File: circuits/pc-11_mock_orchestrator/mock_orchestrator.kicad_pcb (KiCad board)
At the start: 2 copper layers, 99.1 x 99.1 mm, 39 parts, among them Q1 2N7002, Q2 2N7002, Q3 2N7002, SW1 SW_Push, SW10 SW_Push, SW11 SW_Push, SW12 SW_Push, SW13 SW_Push, SW14 SW_Push, SW15 SW_Push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

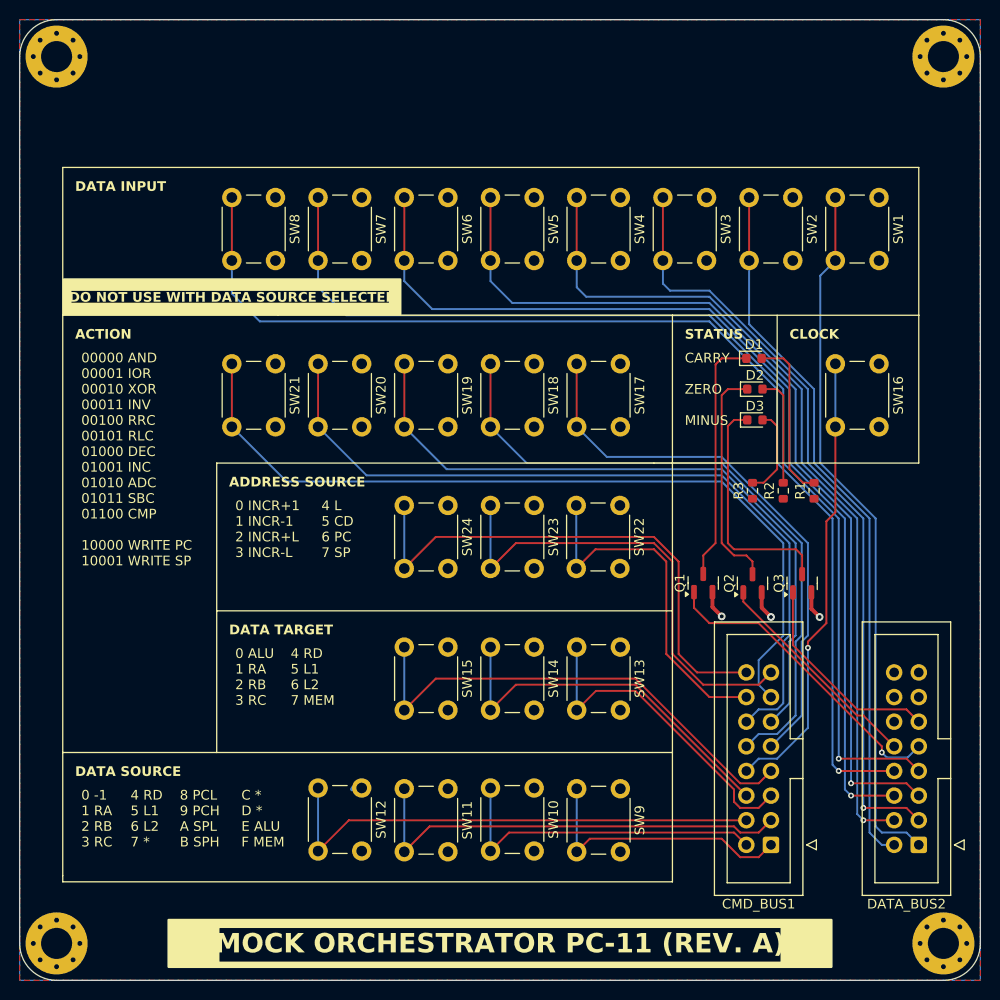
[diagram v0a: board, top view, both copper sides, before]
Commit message: add filter and decoupling capacitors to all boards
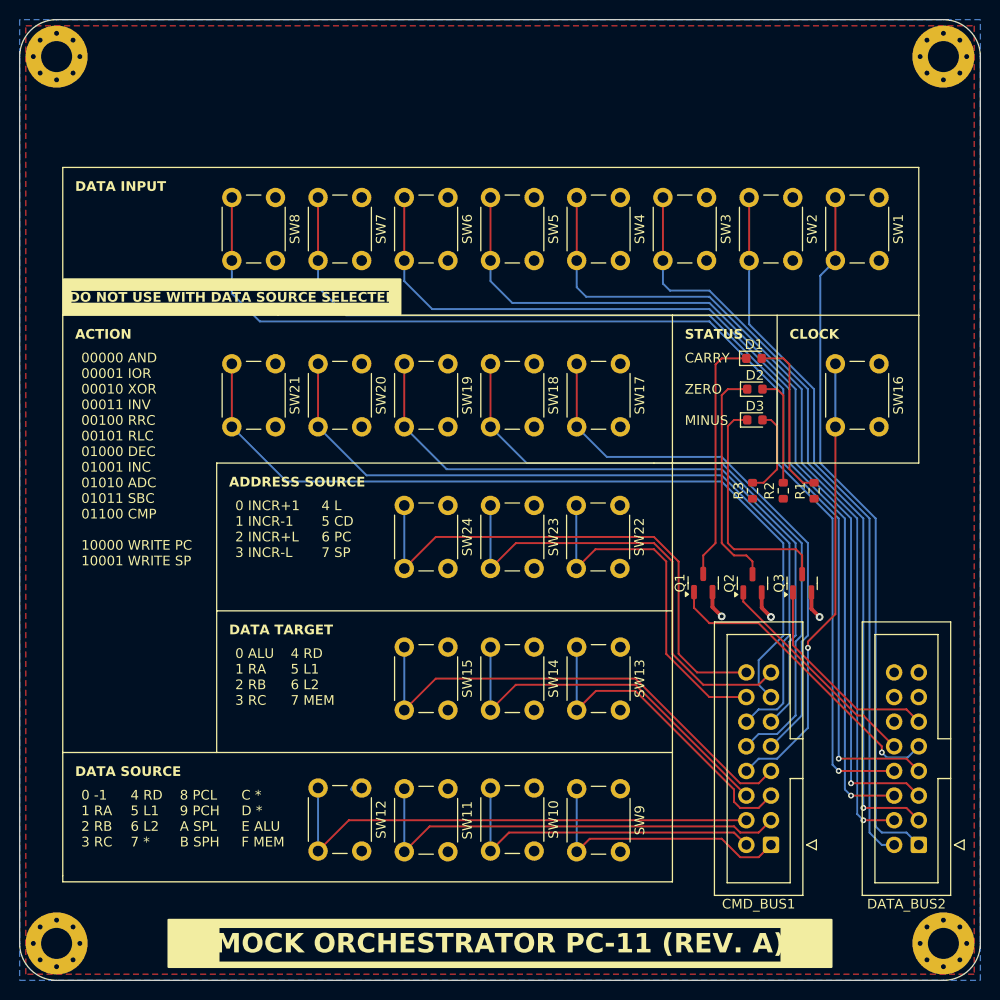
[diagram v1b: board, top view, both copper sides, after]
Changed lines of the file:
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@@
 	)
 	(segment
-		(start 123.825 74.585)
-		(end 124.75 73.66)
-		(width 0.2)
-		(layer "F.Cu")
-		(net 28)
-	)
-	(segment
-		(start 123.825 85.09)
+		(start 121.92 86.995)
+		(end 124.75 84.165)
+		(width 0.2)
+		(layer "F.Cu")
+		(net 28)
+	)
+	(segment
+		(start 124.75 84.165)
+		(end 124.75 64.845)
+		(width 0.2)
+		(layer "F.Cu")
+		(net 28)
+	)
+	(segment
+		(start 121.92 87.63)
 		(end 121.92 86.995)
-		(width 0.2)
-		(layer "F.Cu")
-		(net 28)
-	)
-	(segment
-		(start 123.825 85.09)
-		(end 123.825 74.585)
-		(width 0.2)
-		(layer "F.Cu")
-		(net 28)
-	)
-	(segment
-		(start 121.92 86.995)
-		(end 121.92 87.63)
-		(width 0.2)
-		(layer "F.Cu")
-		(net 28)
-	)
-	(segment
-		(start 124.75 73.66)
-		(end 124.75 64.845)
 		(width 0.2)
 		(layer "F.Cu")
@@
 		(polygon
 			(pts
-				(xy 40.64 22.86) (xy 139.7 22.86) (xy 139.7 121.92) (xy 40.64 121.92)
+				(xy 41.275 23.495) (xy 139.065 23.495) (xy 139.065 121.285) (xy 41.275 121.285)
 			)
 		)

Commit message: final touches, pcb ordering
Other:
- board text added: "DATA INTERCONNECT"
- board text added: "OPERATION INTERCONNECT"
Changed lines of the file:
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@@
 			(disableapertmacros no)
 			(usegerberextensions no)
-			(usegerberattributes yes)
-			(usegerberadvancedattributes yes)
-			(creategerberjobfile yes)
+			(usegerberattributes no)
+			(usegerberadvancedattributes no)
+			(creategerberjobfile no)
 			(dashed_line_dash_ratio 12.000000)
 			(dashed_line_gap_ratio 3.000000)
@@
 			(sketchdnponfab yes)
 			(crossoutdnponfab yes)
-			(subtractmaskfromsilk no)
+			(subtractmaskfromsilk yes)
 			(outputformat 1)
 			(mirror no)
-			(drillshape 1)
+			(drillshape 0)
 			(scaleselection 1)
-			(outputdirectory "")
+			(outputdirectory "./CAM")
 		)
 	)
@@
 		(tags "Through hole vertical IDC box header THT 2x08 2.54mm double row")
 		(property "Reference" "DATA_BUS2"
-			(at 1.27 -6.1 0)
+			(at 1.27 25.4 0)
 			(layer "F.SilkS")
+			(hide yes)
 			(effects
 				(font
@@
 			(at 1.27 -6.1 0)
 			(layer "F.SilkS")
+			(hide yes)
 			(effects
 				(font
@@
 		)
 	)
+	(gr_text "DATA INTERCONNECT"
+		(at 126.365 99.06 90)
+		(layer "F.SilkS")
+		(effects
+			(font
+				(size 1 1)
+				(thickness 0.1)
+			)
+			(justify bottom)
+		)
+	)
 	(gr_text "CARRY\n\nZERO\n\nMINUS"
 		(at 109.22 64.77 0)
@@
 		)
 	)
+	(gr_text "OPERATION INTERCONNECT"
+		(at 111.125 99.06 90)
+		(layer "F.SilkS")
+		(effects
+			(font
+				(size 1 1)
+				(thickness 0.1)
+			)
+			(justify bottom)
+		)
+	)

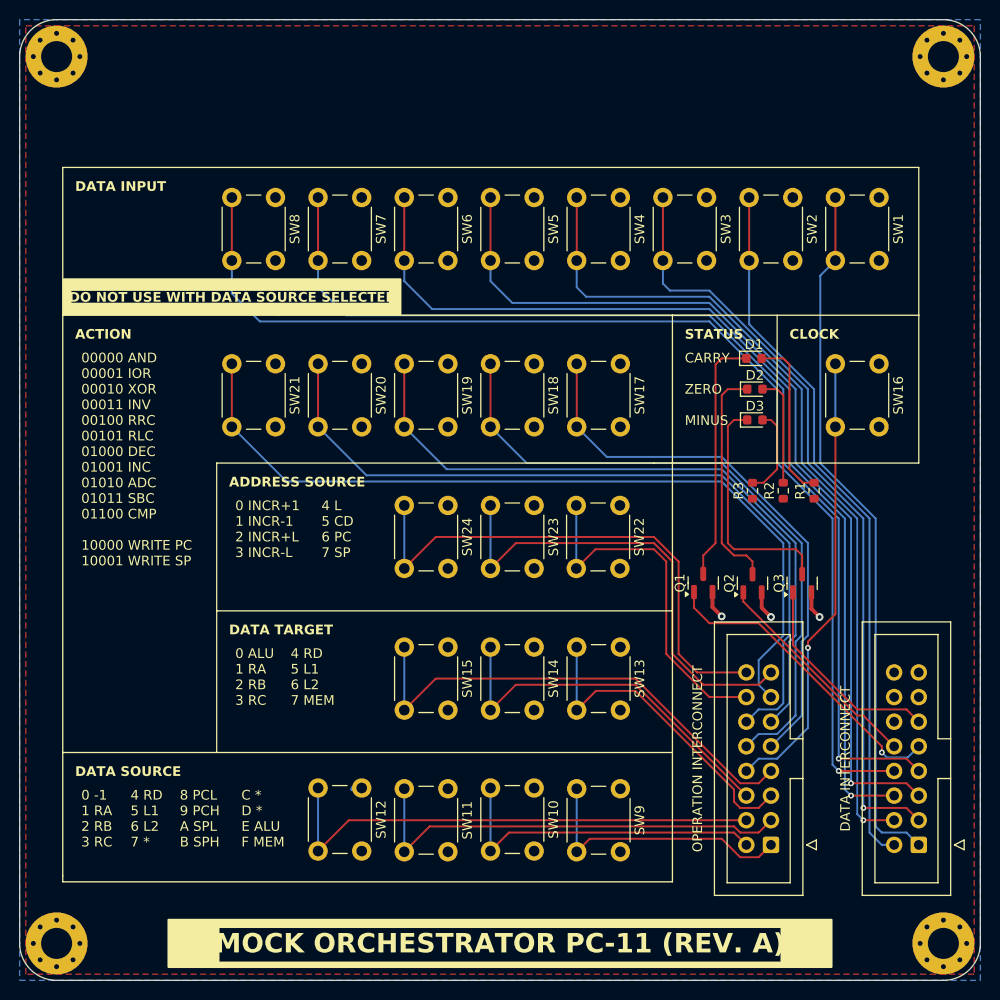
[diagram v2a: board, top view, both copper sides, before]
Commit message: update documentation and update PCBs for interrupts
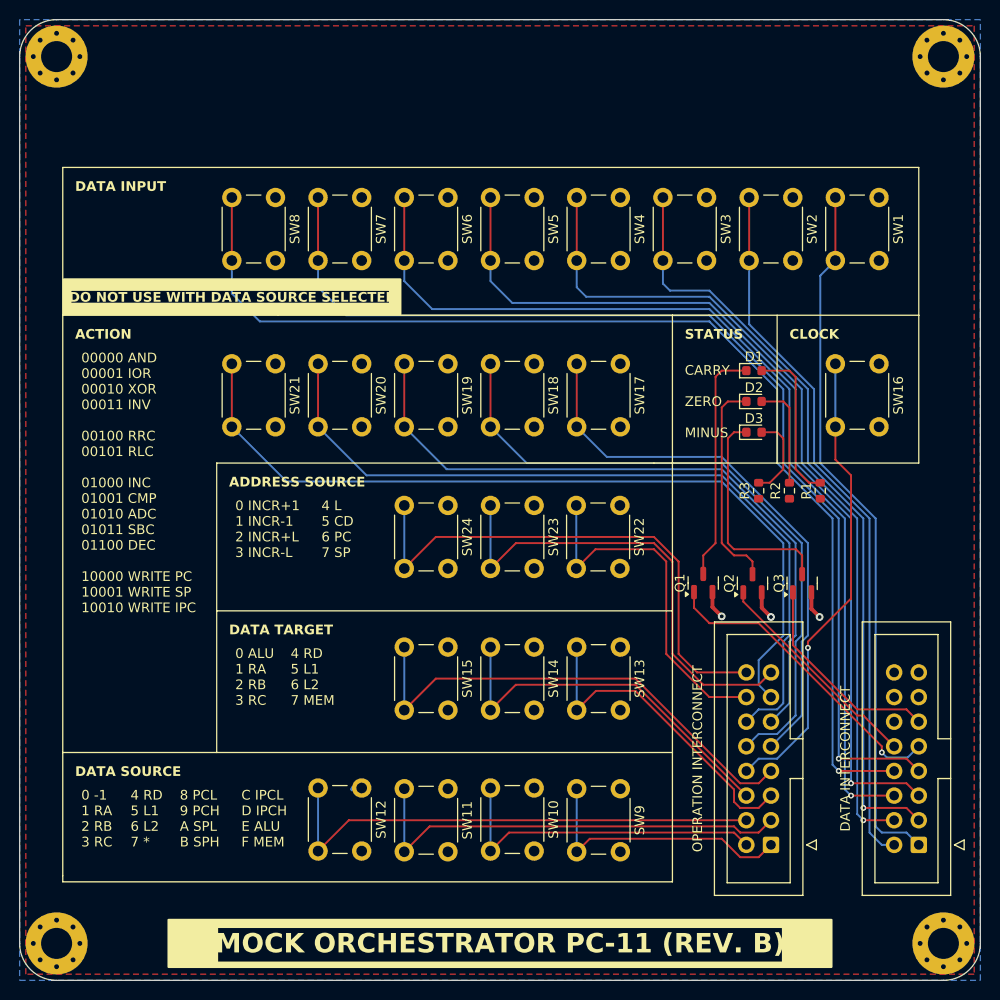
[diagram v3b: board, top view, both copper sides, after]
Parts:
- moved D2 1.27 mm to (116.4, 62.2)
- moved D3 1.27 mm to (116.4, 65.4)
- moved D1 1.27 mm to (116.4, 59.1)
- moved R2 0.64 mm to (120.0, 71.4)
- moved R3 0.64 mm to (116.8, 71.4)
- moved R1 0.63 mm to (123.2, 71.4)
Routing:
- net Net-(D3-K): track 24.4 -> 23.1 mm
- net Net-(D2-K): track 23.4 -> 22.0 mm
- net /clock: track 46.9 -> 48.2 mm
- net Net-(D1-K): track 25.6 -> 24.3 mm
- net Net-(D1-A): track 17.0 -> 16.4 mm
- net Net-(D3-A): track 9.33 -> 8.79 mm
- net Net-(D2-A): track 11.4 -> 10.9 mm
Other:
- board text added: "00000 AND 00001 IOR 00010 XOR 00011 INV 00100 RRC 00101 RLC 01000 INC 01001 CMP 01010 ADC 01011 SBC 01100 DEC 10000 WRITE PC 10001 WRITE SP 10010 WRITE IPC"
- board text added: "C IPCL D IPCH E ALU F MEM"
- board text added: "MOCK ORCHESTRATOR PC-11 (REV. B)"
- board text removed: "00000 AND 00001 IOR 00010 XOR 00011 INV 00100 RRC 00101 RLC 01000 DEC 01001 INC 01010 ADC 01011 SBC 01100 CMP 10000 WRITE PC 10001 WRITE SP"
- board text removed: "C * D * E ALU F MEM"
- board text removed: "MOCK ORCHESTRATOR PC-11 (REV. A)"
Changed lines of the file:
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@@
 	(paper "A4")
 	(title_block
-		(title "Dual 8-Bit Register Unit")
-		(date "2025-02-13")
-		(rev "PC-01-A")
+		(title "Mock Orchestrator")
+		(date "2025-11-04")
+		(rev "PC-11-B")
 	)
 	(layers
@@
 	(footprint "LED_SMD:LED_0603_1608Metric"
 		(layer "F.Cu")
-		(at 116.45 64.135)
+		(at 116.3575 65.405)
 		(descr "LED SMD 0603 (1608 Metric), square (rectangular) end terminal, IPC_7351 nominal, (Body size source: http://www.tortai-tech.com/upload/download/2011102023233369053.pdf), generated with kicad-footprint-generator")
 		(tags "LED")
@@
 	(footprint "Resistor_SMD:R_0603_1608Metric"
 		(layer "F.Cu")
-		(at 116.205 71.437 90)
+		(at 116.84 71.437 90)
 		(descr "Resistor SMD 0603 (1608 Metric), square (rectangular) end terminal, IPC_7351 nominal, (Body size source: IPC-SM-782 page 72, https://www.pcb-3d.com/wordpress/wp-content/uploads/ipc-sm-782a_amendment_1_and_2.pdf), generated with kicad-footprint-generator")
 		(tags "resistor")
@@
 	(footprint "LED_SMD:LED_0603_1608Metric"
 		(layer "F.Cu")
-		(at 116.45 60.96)
+		(at 116.3575 62.23)
 		(descr "LED SMD 0603 (1608 Metric), square (rectangular) end terminal, IPC_7351 nominal, (Body size source: http://www.tortai-tech.com/upload/download/2011102023233369053.pdf), generated with kicad-footprint-generator")
 		(tags "LED")
@@
 	(footprint "LED_SMD:LED_0603_1608Metric"
 		(layer "F.Cu")
-		(at 116.3575 57.785)
+		(at 116.3575 59.055)
 		(descr "LED SMD 0603 (1608 Metric), square (rectangular) end terminal, IPC_7351 nominal, (Body size source: http://www.tortai-tech.com/upload/download/2011102023233369053.pdf), generated with kicad-footprint-generator")
 		(tags "LED")
@@
 	(footprint "Resistor_SMD:R_0603_1608Metric"
 		(layer "F.Cu")
-		(at 122.555 71.437 90)
+		(at 123.19 71.437 90)
 		(descr "Resistor SMD 0603 (1608 Metric), square (rectangular) end terminal, IPC_7351 nominal, (Body size source: IPC-SM-782 page 72, https://www.pcb-3d.com/wordpress/wp-content/uploads/ipc-sm-782a_amendment_1_and_2.pdf), generated with kicad-footprint-generator")
 		(tags "resistor")
@@
 	(footprint "Resistor_SMD:R_0603_1608Metric"
 		(layer "F.Cu")
-		(at 119.38 71.437 90)
+		(at 120.015 71.437 90)
 		(descr "Resistor SMD 0603 (1608 Metric), square (rectangular) end terminal, IPC_7351 nominal, (Body size source: IPC-SM-782 page 72, https://www.pcb-3d.com/wordpress/wp-content/uploads/ipc-sm-782a_amendment_1_and_2.pdf), generated with kicad-footprint-generator")
 		(tags "resistor")
@@
 		(layer "Edge.Cuts")
 	)
-	(gr_text "C *\nD *\nE ALU\nF MEM"
+	(gr_text "C IPCL\nD IPCH\nE ALU\nF MEM"
 		(at 63.5 102.235 0)
 		(layer "F.SilkS")
@@
 	)
 	(gr_text "CARRY\n\nZERO\n\nMINUS"
-		(at 109.22 64.77 0)
+		(at 109.22 66.04 0)
 		(layer "F.SilkS")
 		(effects
@@
 		)
 	)
-	(gr_text "00000 AND\n00001 IOR\n00010 XOR\n00011 INV\n00100 RRC\n00101 RLC\n01000 DEC\n01001 INC\n01010 ADC\n01011 SBC\n01100 CMP\n\n10000 WRITE PC\n10001 WRITE SP"
+	(gr_text "00000 AND\n00001 IOR\n00010 XOR\n00011 INV\n\n00100 RRC\n00101 RLC\n\n01000 INC\n01001 CMP\n01010 ADC\n01011 SBC\n01100 DEC\n\n10000 WRITE PC\n10001 WRITE SP\n10010 WRITE IPC"
 		(at 46.99 57.15 0)
 		(layer "F.SilkS")
@@
 		)
 	)
-	(gr_text "MOCK ORCHESTRATOR PC-11 (REV. A)"
+	(gr_text "MOCK ORCHESTRATOR PC-11 (REV. B)"
 		(at 90.17 118.11 0)
 		(layer "F.SilkS" knockout)
@@
 	)
 	(segment
-		(start 120.015 58.42)
-		(end 120.015 69.215)
+		(start 117.145 59.055)
+		(end 120.015 59.055)
 		(width 0.2)
 		(layer "F.Cu")
@@
 	)
 	(segment
-		(start 121.412 70.612)
-		(end 122.555 70.612)
+		(start 120.65 69.215)
+		(end 120.65 59.69)
 		(width 0.2)
 		(layer "F.Cu")
@@
 	)
 	(segment
-		(start 119.38 57.785)
-		(end 120.015 58.42)
+		(start 122.047 70.612)
+		(end 120.65 69.215)
 		(width 0.2)
 		(layer "F.Cu")
@@
 	)
 	(segment
-		(start 120.015 69.215)
-		(end 121.412 70.612)
+		(start 123.19 70.612)
+		(end 122.047 70.612)
 		(width 0.2)
 		(layer "F.Cu")
@@
 	)
 	(segment
-		(start 117.145 57.785)
-		(end 119.38 57.785)
+		(start 120.015 59.055)
+		(end 120.65 59.69)
 		(width 0.2)
 		(layer "F.Cu")
@@
 	)
 	(segment
-		(start 113.03 57.785)
-		(end 112.395 58.42)
+		(start 115.57 59.055)
+		(end 113.03 59.055)
 		(width 0.2)
 		(layer "F.Cu")
@@
 	)
 	(segment
-		(start 112.395 58.42)
+		(start 112.395 59.69)
 		(end 112.395 76.835)
 		(width 0.2)
@@
 	)
 	(segment
-		(start 115.57 57.785)
-		(end 113.03 57.785)
+		(start 113.03 59.055)
+		(end 112.395 59.69)
 		(width 0.2)
 		(layer "F.Cu")
@@
 	)
 	(segment
+		(start 113.665 62.23)
+		(end 113.03 62.865)
+		(width 0.2)
+		(layer "F.Cu")
+		(net 21)
+	)
+	(segment
 		(start 113.03 76.835)
 		(end 114.3 78.105)
@@
 	)
 	(segment
-		(start 113.03 61.595)
-		(end 113.03 76.835)
-		(width 0.2)
-		(layer "F.Cu")
-		(net 21)
-	)
-	(segment
 		(start 114.3 78.105)
 		(end 115.57 78.105)
@@
 	)
 	(segment
-		(start 115.6625 60.96)
-		(end 113.665 60.96)
+		(start 115.57 62.23)
+		(end 113.665 62.23)
 		(width 0.2)
 		(layer "F.Cu")
@@
 	)
 	(segment
-		(start 113.665 60.96)
-		(end 113.03 61.595)
+		(start 113.03 62.865)
+		(end 113.03 76.835)
 		(width 0.2)
 		(layer "F.Cu")
@@
 	)
 	(segment
-		(start 119.38 70.612)
-		(end 119.38 61.595)
+		(start 120.015 62.865)
+		(end 120.015 70.612)
 		(width 0.2)
 		(layer "F.Cu")
@@
 	)
 	(segment
-		(start 119.38 61.595)
-		(end 118.745 60.96)
+		(start 117.145 62.23)
+		(end 119.38 62.23)
 		(width 0.2)
 		(layer "F.Cu")
@@
 	)
 	(segment
-		(start 118.745 60.96)
-		(end 117.2375 60.96)
+		(start 119.38 62.23)
+		(end 120.015 62.865)
 		(width 0.2)
 		(layer "F.Cu")
@@
 	)
 	(segment
-		(start 114.3 64.135)
-		(end 113.665 64.77)
-		(width 0.2)
-		(layer "F.Cu")
-		(net 23)
-	)
-	(segment
 		(start 120.69 77.47)
 		(end 121.325 78.105)
@@
 	)
 	(segment
-		(start 113.665 64.77)
+		(start 113.665 66.04)
 		(end 113.665 76.835)
 		(width 0.2)
@@
 	)
 	(segment
-		(start 115.6625 64.135)
-		(end 114.3 64.135)
+		(start 115.57 65.405)
+		(end 114.3 65.405)
+		(width 0.2)
+		(layer "F.Cu")
+		(net 23)
+	)
+	(segment
+		(start 114.3 65.405)
+		(end 113.665 66.04)
 		(width 0.2)
 		(layer "F.Cu")
@@
 	)
 	(segment
-		(start 118.745 69.215)
-		(end 118.745 64.77)
+		(start 119.38 69.215)
+		(end 117.983 70.612)
 		(width 0.2)
 		(layer "F.Cu")
@@
 	)
 	(segment
-		(start 118.11 64.135)
-		(end 117.2375 64.135)
+		(start 117.983 70.612)
+		(end 116.84 70.612)
 		(width 0.2)
 		(layer "F.Cu")
@@
 	)
 	(segment
-		(start 118.745 64.77)
-		(end 118.11 64.135)
+		(start 118.745 65.405)
+		(end 119.38 66.04)
 		(width 0.2)
 		(layer "F.Cu")
@@
 	)
 	(segment
-		(start 117.348 70.612)
-		(end 118.745 69.215)
+		(start 117.145 65.405)
+		(end 118.745 65.405)
 		(width 0.2)
 		(layer "F.Cu")
@@
 	)
 	(segment
-		(start 116.205 70.612)
-		(end 117.348 70.612)
+		(start 119.38 66.04)
+		(end 119.38 69.215)
 		(width 0.2)
 		(layer "F.Cu")
@@
 	(segment
 		(start 121.92 86.995)
-		(end 124.75 84.165)
+		(end 121.92 87.63)
+		(width 0.2)
+		(layer "F.Cu")
+		(net 28)
+	)
+	(segment
+		(start 126.365 69.85)
+		(end 126.365 82.55)
+		(width 0.2)
+		(layer "F.Cu")
+		(net 28)
+	)
+	(segment
+		(start 124.75 68.235)
+		(end 126.365 69.85)
 		(width 0.2)
 		(layer "F.Cu")
@@
 	)
 	(segment
-		(start 124.75 84.165)
-		(end 124.75 64.845)
+		(start 124.75 64.845)
+		(end 124.75 68.235)
 		(width 0.2)
 		(layer "F.Cu")
@@
 	)
 	(segment
-		(start 121.92 87.63)
+		(start 126.365 82.55)
 		(end 121.92 86.995)
 		(width 0.2)
